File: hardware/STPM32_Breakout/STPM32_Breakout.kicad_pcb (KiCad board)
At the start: 2 copper layers, 55 x 40 mm, 5 parts, among them U1 STPM32

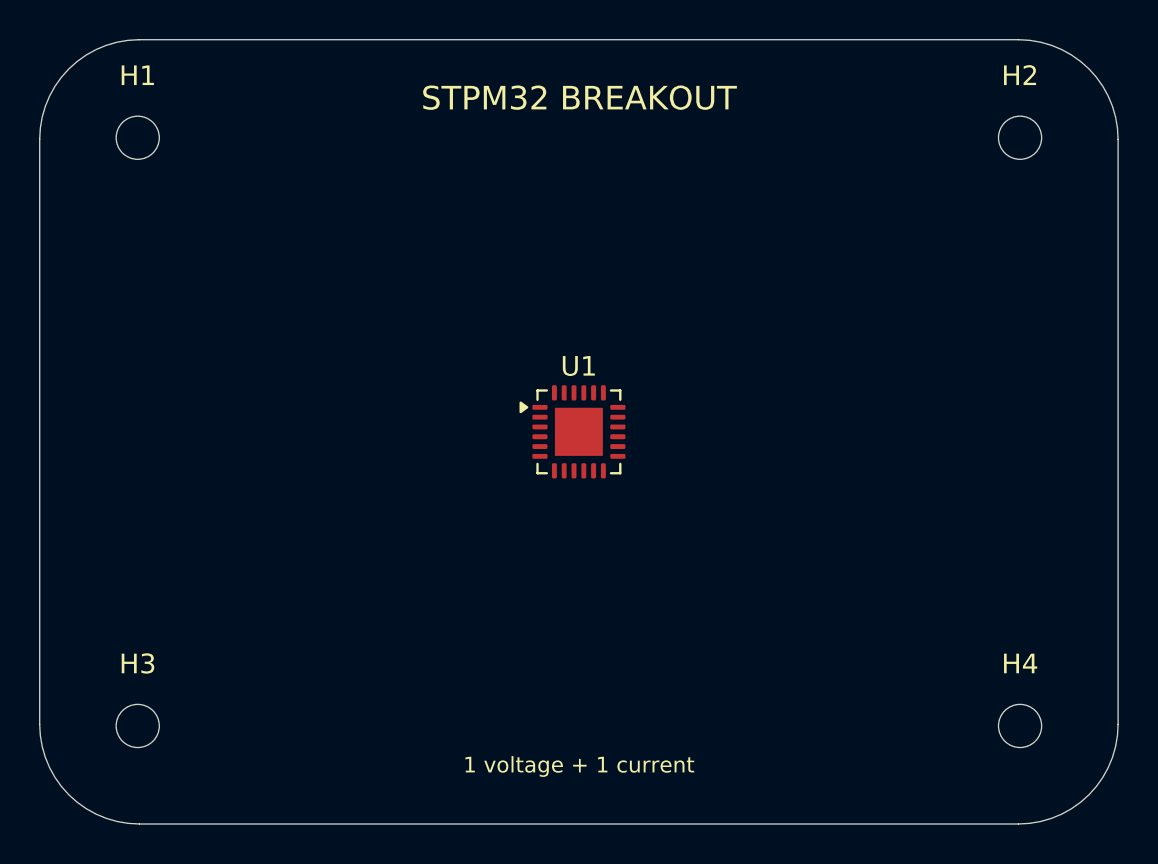
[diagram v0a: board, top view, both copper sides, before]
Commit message: Complete compact STPM32 breakout
Implement the isolated 9 VAC and current-output CT front end, compact breadboard PCB, routed ground planes, validation scripts, and design documentation.

Co-authored-by: Copilot <223556219+Copilot@users.noreply.github.com>
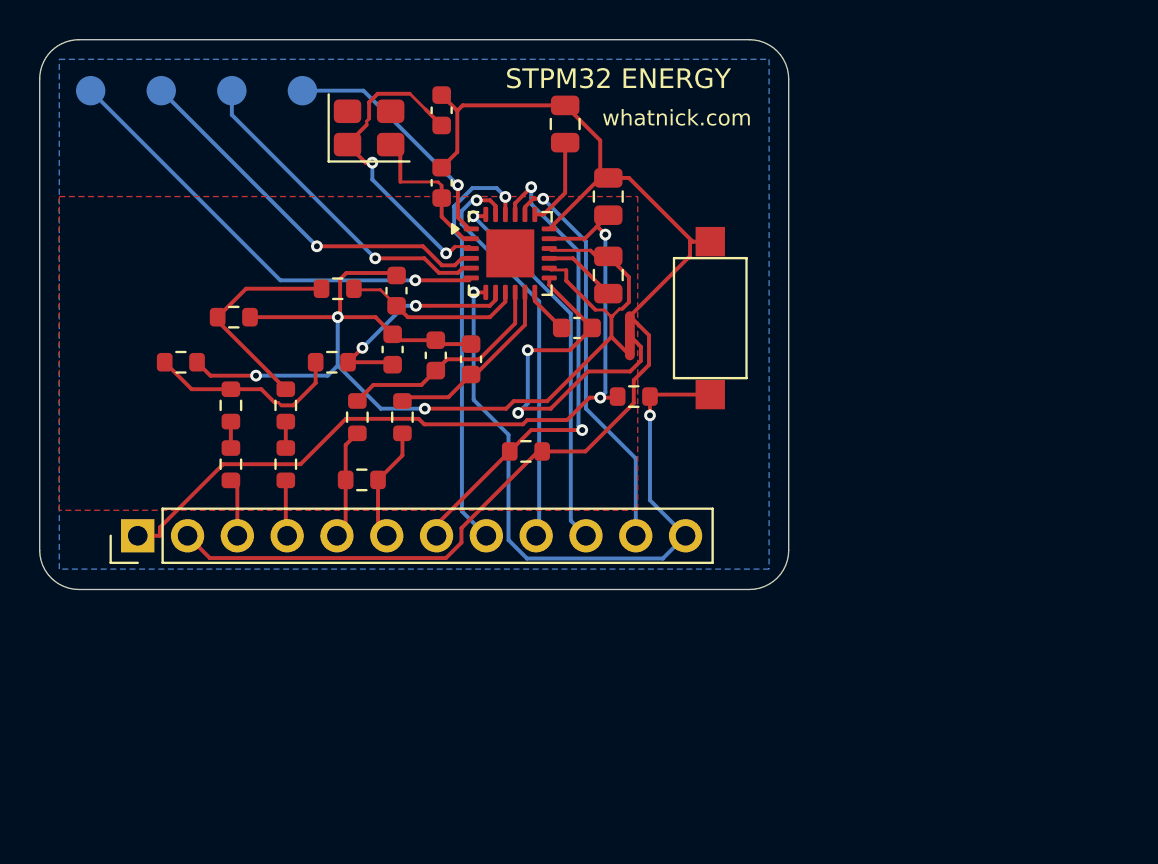
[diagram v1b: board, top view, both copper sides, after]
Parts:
- removed H1, H2, H3, H4: M2, MountingHole_2.2mm_M2
- added C1: 330n, C_0603_1608Metric, F.Cu at (40.2, 36.1)
- added C10: 1u, C_0805_2012Metric, F.Cu at (49.0, 32.0)
- added C11: 4.7u, C_0805_2012Metric, F.Cu at (46.8, 24.3)
- added C12: 100n, C_0603_1608Metric, F.Cu at (47.4, 34.7)
- added C13: 15p, C_0603_1608Metric, F.Cu at (40.5, 23.6)
- added C14: 15p, C_0603_1608Metric, F.Cu at (40.5, 27.3)
- added C2: 330n, C_0603_1608Metric, F.Cu at (42.0, 36.3)
- added C3: 33n, C_0603_1608Metric, F.Cu at (38.0, 35.8)
- added C4: 33n, C_0603_1608Metric, F.Cu at (38.2, 32.8)
- added C9: 1u, C_0805_2012Metric, F.Cu at (49.0, 28.0)
- added J1: BREADBOARD I/O, PinHeader_1x12_P2.54mm_Vertical, F.Cu at (25.0, 45.3)
- added NT1: ANALOG/DIGITAL STAR, NetTie-3_SMD_Pad0.5mm, F.Cu at (50.1, 35.1)
- added R1: 100R, R_0603_1608Metric, F.Cu at (36.2, 39.2)
- added R10: 1k, R_0603_1608Metric, F.Cu at (35.2, 32.7)
- added R11: 10k, R_0603_1608Metric, F.Cu at (50.3, 38.2)
- added R12: 10k, R_0603_1608Metric, F.Cu at (44.8, 41.0)
- added R2: 100R, R_0603_1608Metric, F.Cu at (38.5, 39.2)
- added R3: 100k, R_0603_1608Metric, F.Cu at (29.8, 41.6)
- added R4: 100k, R_0603_1608Metric, F.Cu at (29.8, 38.6)
- added R5: 2.49k, R_0603_1608Metric, F.Cu at (27.2, 36.5)
- added R6: 100k, R_0603_1608Metric, F.Cu at (32.5, 41.6)
- added R7: 100k, R_0603_1608Metric, F.Cu at (32.5, 38.6)
- added R8: 2.49k, R_0603_1608Metric, F.Cu at (29.9, 34.1)
- added R9: 1k, R_0603_1608Metric, F.Cu at (34.9, 36.5)
- added RB1: 2.4R, R_0603_1608Metric, F.Cu at (36.4, 42.5)
- added SW1: RESET, SW_SPST_CK_RS282G05A3, F.Cu at (54.2, 34.2)
- added TP1: INT1, TestPoint_Pad_D1.5mm, B.Cu at (22.6, 22.6)
- added TP2: LED1, TestPoint_Pad_D1.5mm, B.Cu at (26.2, 22.6)
- added TP3: LED2, TestPoint_Pad_D1.5mm, B.Cu at (29.8, 22.6)
- added TP4: CLKOUT_ZCR, TestPoint_Pad_D1.5mm, B.Cu at (33.4, 22.6)
- added Y1: 16MHz, Crystal_SMD_3225-4Pin_3.2x2.5mm, F.Cu at (36.8, 24.5)
- moved U1 9.75 mm to (44.0, 30.9)
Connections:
- U1 pad 1: (no net) -> CLKOUT_ZCR
- U1 pad 10: (no net) -> IIP1
- U1 pad 11: (no net) -> IIN1
- U1 pad 12: (no net) -> VREF1
- U1 pad 13: (no net) -> GND_REF
- U1 pad 14: (no net) -> AGND
- U1 pad 15: (no net) -> VDDA
- U1 pad 16: (no net) -> AGND
- U1 pad 17: (no net) -> +3V3
- U1 pad 18: (no net) -> DGND
- U1 pad 19: (no net) -> VDDD
- U1 pad 2: (no net) -> XTAL2
- U1 pad 20: (no net) -> SYN
- U1 pad 21: (no net) -> SCS
- U1 pad 22: (no net) -> SCL
- U1 pad 23: (no net) -> MOSI_RXD
- U1 pad 24: (no net) -> MISO_TXD
- U1 pad 3: (no net) -> XTAL1
- U1 pad 4: (no net) -> LED1
- U1 pad 5: (no net) -> LED2
- U1 pad 6: (no net) -> INT1
- U1 pad 7: (no net) -> EN
- U1 pad 8: (no net) -> VIP1
- U1 pad 9: (no net) -> VIN1
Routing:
- net DGND: track 0.00 -> 62.4 mm
- net AGND: track 0.00 -> 57.4 mm, vias 0 -> 3
- net +3V3: track 0.00 -> 40.4 mm, vias 0 -> 2
- net EN: track 0.00 -> 34.9 mm, vias 0 -> 2
- net SCS: track 0.00 -> 25.2 mm, vias 0 -> 2
- net INT1: track 0.00 -> 23.5 mm, vias 0 -> 1
- net SCL: track 0.00 -> 21.6 mm, vias 0 -> 1
- net MOSI_RXD: track 0.00 -> 20.8 mm, vias 0 -> 1
- net SYN: track 0.00 -> 20.6 mm, vias 0 -> 1
- net LED1: track 0.00 -> 19.7 mm, vias 0 -> 1
- net GND_REF: track 0.00 -> 19.5 mm, vias 0 -> 2
- net MISO_TXD: track 0.00 -> 19.4 mm, vias 0 -> 1
- net LED2: track 0.00 -> 16.9 mm, vias 0 -> 1
- net XTAL1: track 0.00 -> 16.5 mm, vias 0 -> 2
- net CLKOUT_ZCR: track 0.00 -> 12.5 mm, vias 0 -> 1
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- added copper zone on F.Cu, net AGND
- added copper zone on B.Cu, net DGND
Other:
- board size 55 x 40 mm -> 38.2 x 28 mm
- board text added: "ISOLATED 9 VAC + CT ONLY"
- board text added: "NOT FOR DIRECT MAINS"
- board text added: "STPM32 ENERGY"
- board text added: "TAPR OHL 1.0"
- board text added: "whatnick.com"
- board text removed: "1 voltage + 1 current"
- board text removed: "ANALOG INPUT / FILTER ZONE"
- board text removed: "POWER / DIGITAL I/O ZONE"
- board text removed: "STPM32 BREAKOUT"
- board text removed: "whatnick.com | TAPR OHL | NOT ISOLATED"

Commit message: Add production STPM32 silkscreen
Mark fitted components and signals, add project-local Whatnick and OSHW artwork, and include release and safety identifiers through a reproducible KiCad script.

Co-authored-by: Copilot <223556219+Copilot@users.noreply.github.com>
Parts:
- added LOGO_OSHW: OSHW_Logo, OSHW_Logo, B.Cu at (54.4, 25.0)
- added LOGO_W: Whatnick_Logo, Whatnick_Logo, F.Cu at (23.7, 25.0)
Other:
- board text added: "3V3"
- board text added: "9VAC + CT ONLY"
- board text added: "CLK/ZCR"
- board text added: "CT+"
- board text added: "CT-"
- board text added: "EN"
- board text added: "GND"
- board text added: "INT1"
- board text added: "LED1"
- board text added: "LED2"
- board text added: "MISO"
- board text added: "MOSI"
- board text added: "SCL"
- board text added: "SCS"
- board text added: "SYN"
- board text added: "VAC+"
- board text added: "VAC-"
- board text added: "v1.0 2026-10-05"
- board text removed: "ISOLATED 9 VAC + CT ONLY"
